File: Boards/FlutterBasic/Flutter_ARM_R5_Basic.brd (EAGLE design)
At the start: 68.3 x 26.4 mm, 79 parts, among them U1 MIC5235-3.3, U2 CC1200, U3 SAM3S4/2/1A_48PIN_LQFP, U4 MCP73831, U5 BALUN_CC1200, U6 ATSHA204/ATECC108UDFN, U7 U.FL, X1 12MHz, X2 40MHz

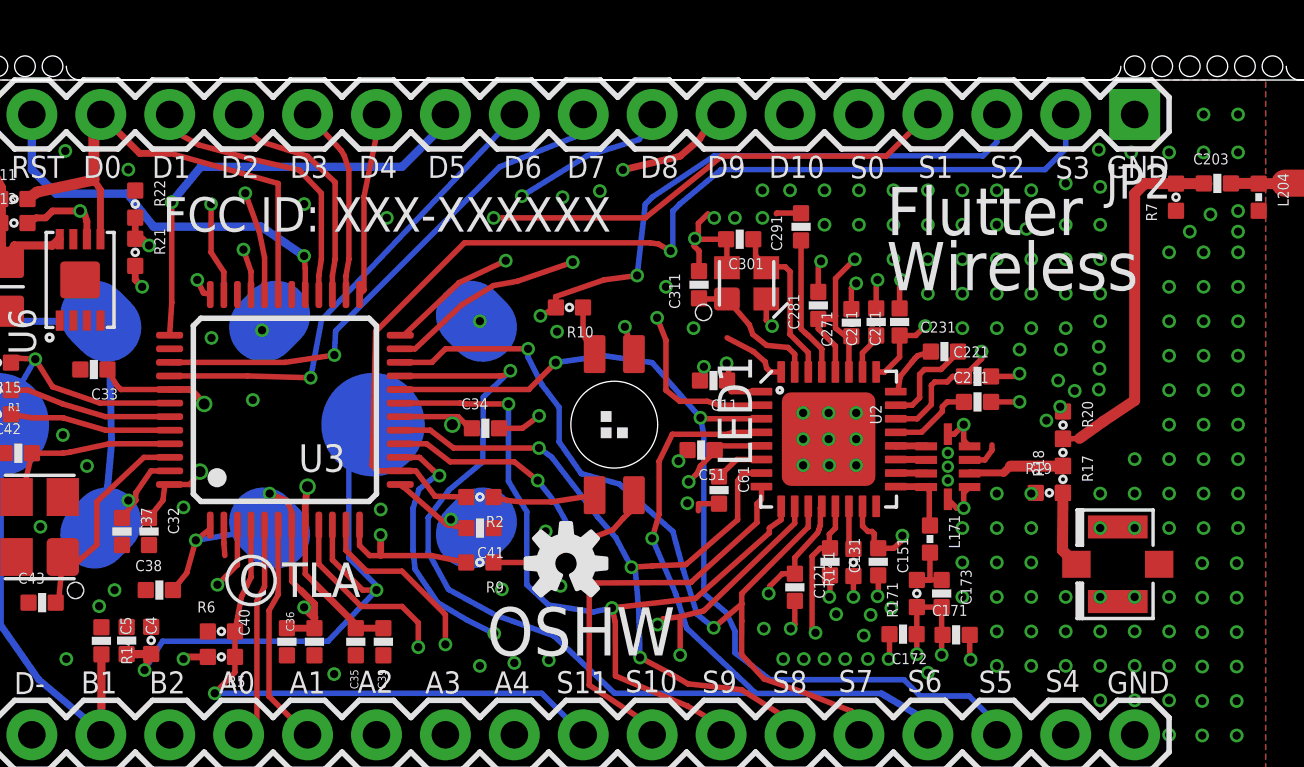
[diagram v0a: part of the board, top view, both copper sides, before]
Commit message: Reorganized schematic, generated PDF schematic.
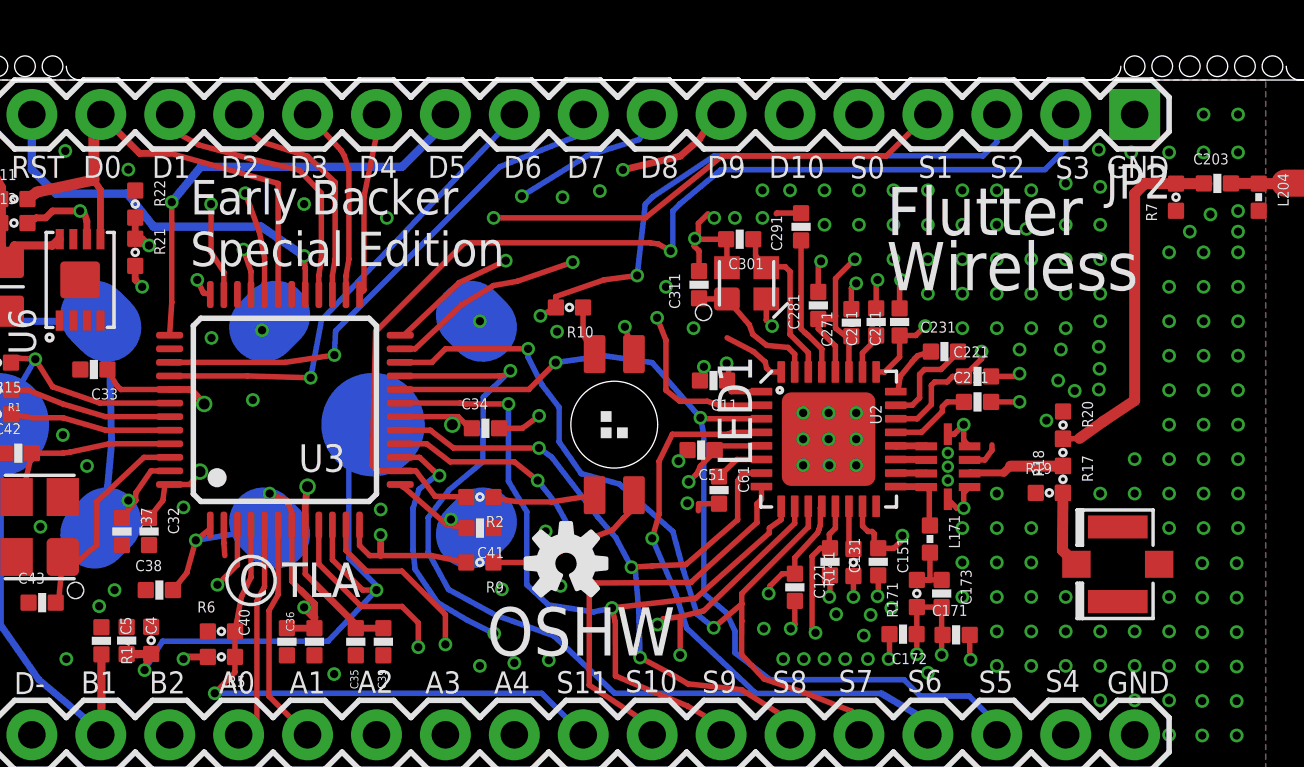
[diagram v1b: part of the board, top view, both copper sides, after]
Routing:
- net GND: vias 219 -> 213
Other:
- board text added: "Early Backer Special Edition"
- board text removed: "FCC ID: XXX-XXXXXX"
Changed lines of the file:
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@@
 <layer number="23" name="tOrigins" color="15" fill="1" visible="yes" active="yes"/>
 <layer number="24" name="bOrigins" color="15" fill="1" visible="yes" active="yes"/>
-<layer number="25" name="tNames" color="7" fill="1" visible="yes" active="yes"/>
-<layer number="26" name="bNames" color="7" fill="1" visible="yes" active="yes"/>
-<layer number="27" name="tValues" color="7" fill="1" visible="yes" active="yes"/>
-<layer number="28" name="bValues" color="7" fill="1" visible="yes" active="yes"/>
+<layer number="25" name="tNames" color="7" fill="1" visible="no" active="yes"/>
+<layer number="26" name="bNames" color="7" fill="1" visible="no" active="yes"/>
+<layer number="27" name="tValues" color="7" fill="1" visible="no" active="yes"/>
+<layer number="28" name="bValues" color="7" fill="1" visible="no" active="yes"/>
 <layer number="29" name="tStop" color="7" fill="3" visible="no" active="yes"/>
 <layer number="30" name="bStop" color="7" fill="6" visible="no" active="yes"/>
@@
 <layer number="44" name="Drills" color="7" fill="1" visible="no" active="yes"/>
 <layer number="45" name="Holes" color="7" fill="1" visible="no" active="yes"/>
-<layer number="46" name="Milling" color="3" fill="1" visible="no" active="yes"/>
+<layer number="46" name="Milling" color="3" fill="1" visible="yes" active="yes"/>
 <layer number="47" name="Measures" color="7" fill="1" visible="no" active="yes"/>
 <layer number="48" name="Document" color="7" fill="1" visible="no" active="yes"/>
@@
 <rectangle x1="51.758571875" y1="19.780246875" x2="51.794128125" y2="19.798028125" layer="22" rot="R270"/>
 <rectangle x1="51.78524375" y1="19.77135625" x2="51.80301875" y2="19.7891375" layer="22" rot="R270"/>
-<text x="14.986" y="19.812" size="1.27" layer="21" font="vector" ratio="20">FCC ID: XXX-XXXXXX</text>
+<text x="16.002" y="18.542" size="1.27" layer="21" font="vector" ratio="20">Early Backer
+Special Edition</text>
 <hole x="6.858" y="25.908" drill="0.762"/>
 <hole x="7.874" y="25.908" drill="0.762"/>
@@
 <vertex x="0" y="25.4"/>
 </polygon>
-<via x="48.0568" y="13.3604" extent="1-16" drill="0.3048"/>
 <via x="49.4792" y="13.9954" extent="1-16" drill="0.3048"/>
 <via x="49.4792" y="15.5702" extent="1-16" drill="0.3048"/>
@@
 <via x="48.26" y="21.59" extent="1-16" drill="0.3048"/>
 <via x="46.99" y="21.336" extent="1-16" drill="0.3048"/>
-<via x="50.8" y="8.89" extent="1-16" drill="0.3048"/>
-<via x="50.8" y="6.35" extent="1-16" drill="0.3048"/>
 <via x="50.8" y="5.08" extent="1-16" drill="0.3048"/>
 <via x="49.53" y="17.526" extent="1-16" drill="0.3048"/>
@@
 <via x="54.61" y="8.89" extent="1-16" drill="0.3048"/>
 <via x="45.72" y="10.16" extent="1-16" drill="0.3048"/>
-<via x="46.99" y="10.16" extent="1-16" drill="0.3048"/>
 <via x="49.53" y="10.16" extent="1-16" drill="0.3048"/>
 <via x="48.26" y="6.35" extent="1-16" drill="0.3048"/>
 <via x="48.26" y="5.08" extent="1-16" drill="0.3048"/>
 <via x="48.26" y="3.81" extent="1-16" drill="0.3048"/>
-<via x="49.53" y="6.35" extent="1-16" drill="0.3048"/>
 <via x="49.53" y="5.08" extent="1-16" drill="0.3048"/>
 <via x="49.53" y="3.81" extent="1-16" drill="0.3048"/>
-<via x="49.53" y="8.89" extent="1-16" drill="0.3048"/>
 <via x="46.99" y="7.62" extent="1-16" drill="0.3048"/>
 <via x="45.72" y="8.89" extent="1-16" drill="0.3048"/>
